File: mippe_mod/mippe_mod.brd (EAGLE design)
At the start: 32.5 x 50 mm, 21 parts, among them J1 VCC, J12 BURNIN, J3 UART, J4 FTDI, SW1 BTN-PTS810, U1 LM340MPX-5.0230, U2 ATMEGA328P-AUR, Y1 16MHz

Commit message: finish module and diff module
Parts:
- added J5: VCC, scono:1X02
- added J6: GND, scono:1X02
- added TP1: TEST_POINTTHRU, scono:TEST_POINT
- J2: value (none) -> GND
- R1: value (none) -> 10k
- R2, R3: value 330R -> 500R
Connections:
- new net AREF: U2.20
- net 5V: now also TP1.1; no longer U2.20
- net GND: now also J6.1, J6.2
- net VCC: now also J5.1, J5.2
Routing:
- net VCC: track 13.7 -> 40.3 mm
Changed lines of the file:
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@@
 <layer number="45" name="Holes" color="3" fill="1" visible="no" active="yes"/>
 <layer number="46" name="Milling" color="3" fill="1" visible="no" active="yes"/>
-<layer number="47" name="Measures" color="15" fill="1" visible="no" active="yes"/>
+<layer number="47" name="Measures" color="15" fill="1" visible="yes" active="yes"/>
 <layer number="48" name="Document" color="7" fill="1" visible="yes" active="yes"/>
 <layer number="49" name="Reference" color="7" fill="1" visible="no" active="yes"/>
@@
 <wire x1="1.5" y1="50" x2="0" y2="48.5" width="0" layer="20"/>
 <wire x1="0" y1="48.5" x2="0" y2="35" width="0" layer="20"/>
-<text x="1.5" y="23.5" size="0.7" layer="21">VCC</text>
-<text x="29.25" y="23.5" size="0.7" layer="21">GND</text>
-<dimension x1="0" y1="7" x2="32.5" y2="7" x3="16.25" y3="-2.5" textsize="0.7" layer="21"/>
-<dimension x1="0" y1="0" x2="0" y2="50" x3="-3.25" y3="25" textsize="0.7" layer="21"/>
+<text x="1.5" y="17" size="0.7" layer="21">VCC</text>
+<text x="29.25" y="17" size="0.7" layer="21">GND</text>
+<dimension x1="0" y1="7" x2="32.5" y2="7" x3="16.25" y3="-2.5" textsize="2" layer="47"/>
+<dimension x1="0" y1="0" x2="0" y2="50" x3="-3.25" y3="25" textsize="2" layer="47"/>
+<dimension x1="3.5" y1="29.5" x2="29" y2="29.5" x3="16.25" y3="53.75" textsize="2" layer="47"/>
+<dimension x1="3.5" y1="29.5" x2="3.5" y2="46.5" x3="40.75" y3="38" textsize="2" layer="47"/>
 </plain>
 <attributes>
@@
 </element>
 <element name="C7" library="scono" library_urn="urn:adsk.eagle:library:14850048" package="0402-CAP" package3d_urn="urn:adsk.eagle:package:14850678/2" value="0.1uF" x="25.75" y="7.5" smashed="yes" rot="R180">
-<attribute name="NAME" x="27.02" y="6.738" size="0.508" layer="25" font="vector" ratio="10" rot="R180"/>
 <attribute name="PIE-INT-REF-NUM" value="CAPACITOR-GENERIC" x="-4.73" y="44.33" size="1.778" layer="27" rot="R180" display="off"/>
 <attribute name="VALUE" x="27.02" y="8.897" size="0.508" layer="27" font="vector" rot="R180"/>
@@
 </element>
 <element name="J12" library="scono" library_urn="urn:adsk.eagle:library:14850048" package="BURNIN" package3d_urn="urn:adsk.eagle:package:14850856/2" value="BURNIN" x="17.72" y="4.77" smashed="yes" rot="R180"/>
-<element name="J2" library="scono" library_urn="urn:adsk.eagle:library:14850048" package="1X02" package3d_urn="urn:adsk.eagle:package:38039/1" value="" x="30.25" y="22" smashed="yes" rot="R270">
+<element name="J2" library="scono" library_urn="urn:adsk.eagle:library:14850048" package="1X02" package3d_urn="urn:adsk.eagle:package:38039/1" value="GND" x="30.25" y="22" smashed="yes" rot="R270">
 <attribute name="VALUE" x="28.218" y="23.27" size="0.6096" layer="27" font="vector" ratio="20" rot="R270"/>
 </element>
@@
 <attribute name="VALUE" x="8.73" y="5.468" size="0.6096" layer="27" font="vector" ratio="20"/>
 </element>
-<element name="R1" library="scono" library_urn="urn:adsk.eagle:library:14850048" package="R0402" package3d_urn="urn:adsk.eagle:package:14850590/2" value="" x="22.5" y="14.25" smashed="yes" rot="R270">
+<element name="R1" library="scono" library_urn="urn:adsk.eagle:library:14850048" package="R0402" package3d_urn="urn:adsk.eagle:package:14850590/2" value="10k" x="22.5" y="14.25" smashed="yes" rot="R270">
 <attribute name="VALUE" x="21.484" y="15.52" size="0.508" layer="27" font="vector" rot="R270" align="top-left"/>
 </element>
-<element name="R2" library="scono" library_urn="urn:adsk.eagle:library:14850048" package="R0402" package3d_urn="urn:adsk.eagle:package:14850590/2" value="330R" x="21.25" y="11" smashed="yes" rot="R90">
+<element name="R2" library="scono" library_urn="urn:adsk.eagle:library:14850048" package="R0402" package3d_urn="urn:adsk.eagle:package:14850590/2" value="500R" x="21.25" y="11" smashed="yes" rot="R90">
 <attribute name="VALUE" x="22.266" y="9.73" size="0.508" layer="27" font="vector" rot="R90" align="top-left"/>
 </element>
-<element name="R3" library="scono" library_urn="urn:adsk.eagle:library:14850048" package="R0402" package3d_urn="urn:adsk.eagle:package:14850590/2" value="330R" x="11.25" y="11" smashed="yes" rot="R270">
+<element name="R3" library="scono" library_urn="urn:adsk.eagle:library:14850048" package="R0402" package3d_urn="urn:adsk.eagle:package:14850590/2" value="500R" x="11.25" y="11" smashed="yes" rot="R270">
 <attribute name="VALUE" x="10.234" y="12.27" size="0.508" layer="27" font="vector" rot="R270" align="top-left"/>
 </element>
@@
 </element>
 <element name="Y1" library="scono" package="XTAL500X320X130N" value="16MHz" x="26" y="22" smashed="yes" rot="R270" grouprefs="XTAL"/>
+<element name="J5" library="scono" library_urn="urn:adsk.eagle:library:14850048" package="1X02" package3d_urn="urn:adsk.eagle:package:38039/1" value="VCC" x="2" y="46" smashed="yes" rot="R45">
+<attribute name="VALUE" x="2.5388125" y="43.66513125" size="0.6096" layer="27" font="vector" ratio="20" rot="R45"/>
+</element>
+<element name="J6" library="scono" library_urn="urn:adsk.eagle:library:14850048" package="1X02" package3d_urn="urn:adsk.eagle:package:38039/1" value="GND" x="30.5" y="46" smashed="yes" rot="R135">
+<attribute name="VALUE" x="32.83486875" y="46.5388125" size="0.6096" layer="27" font="vector" ratio="20" rot="R135"/>
+</element>
+<element name="TP1" library="scono" library_urn="urn:adsk.eagle:library:14850048" package="TEST_POINT" package3d_urn="urn:adsk.eagle:package:14850798/1" value="TEST_POINTTHRU" x="5.5" y="6" smashed="yes"/>
 </elements>
 <signals>
@@
 <wire x1="11.627" y1="9" x2="11.25" y2="9" width="0.1524" layer="1"/>
 <via x="11.25" y="9" extent="1-16" drill="0.35"/>
+<contactref element="J6" pad="1"/>
+<contactref element="J6" pad="2"/>
 </signal>
 <signal name="SCL">
@@
 <via x="13.804075" y="24.554075" extent="1-16" drill="0.35"/>
 <wire x1="13.804075" y1="24.554075" x2="13.804075" y2="20.054075" width="0.1524" layer="16"/>
-<wire x1="13.2768" y1="19.5268" x2="13.804075" y2="20.054075" width="0.1524" layer="16"/>
+<wire x1="13.375" y1="19.625" x2="13.2768" y2="19.5268" width="0.1524" layer="16"/>
+<wire x1="13.375" y1="19.625" x2="13.804075" y2="20.054075" width="0.1524" layer="16"/>
 <wire x1="17.72" y1="2.23" x2="16.75" y2="3.2" width="0.1524" layer="16"/>
 <wire x1="16.75" y1="3.2" x2="16.75" y2="4.5" width="0.1524" layer="16"/>
 <wire x1="16.75" y1="4.5" x2="15.25" y2="6" width="0.1524" layer="16"/>
-<wire x1="13.7084" y1="7.98396875" x2="13.2768" y2="8.41556875" width="0.1524" layer="16"/>
-<wire x1="13.2768" y1="8.41556875" x2="13.2768" y2="19.5268" width="0.1524" layer="16"/>
-<wire x1="13.7084" y1="6.5416" x2="13.7084" y2="7.98396875" width="0.1524" layer="16"/>
-<wire x1="15.25" y1="6" x2="14.25" y2="6" width="0.1524" layer="16"/>
-<wire x1="14.25" y1="6" x2="13.7084" y2="6.5416" width="0.1524" layer="16"/>
+<wire x1="14.25" y1="6" x2="15.25" y2="6" width="0.1524" layer="16"/>
+<wire x1="13.2768" y1="19.5268" x2="13.2768" y2="8.9732" width="0.1524" layer="16"/>
+<wire x1="13.2768" y1="8.9732" x2="13.75" y2="8.5" width="0.1524" layer="16"/>
+<wire x1="13.75" y1="8.5" x2="13.75" y2="6.5" width="0.1524" layer="16"/>
+<wire x1="13.75" y1="6.5" x2="14.25" y2="6" width="0.1524" layer="16"/>
 </signal>
 <signal name="SCK">
@@
 <contactref element="U2" pad="6"/>
 <contactref element="U2" pad="18"/>
-<contactref element="U2" pad="20"/>
 <contactref element="J4" pad="4"/>
 <contactref element="U1" pad="3"/>
@@
 <wire x1="17.72" y1="4.77" x2="17.72" y2="7.4" width="0.1524" layer="16"/>
 <wire x1="17.72" y1="7.4" x2="17.62" y2="7.5" width="0.1524" layer="16"/>
+<contactref element="TP1" pad="1"/>
 </signal>
 <signal name="VCC">
@@
 <wire x1="8.9" y1="19.85" x2="6.75" y2="22" width="0.508" layer="1"/>
 <wire x1="2.25" y1="19.46" x2="2.25" y2="22" width="0.508" layer="1"/>
+<contactref element="J5" pad="2"/>
+<contactref element="J5" pad="1"/>
+<wire x1="3.79605" y1="47.79605" x2="2" y2="46" width="0.508" layer="1"/>
+<wire x1="2" y1="46" x2="2" y2="22.25" width="0.508" layer="1"/>
+<wire x1="2" y1="22.25" x2="2.25" y2="22" width="0.508" layer="1"/>
+</signal>
+<signal name="AREF">
+<contactref element="U2" pad="20"/>
 </signal>
 </signals>

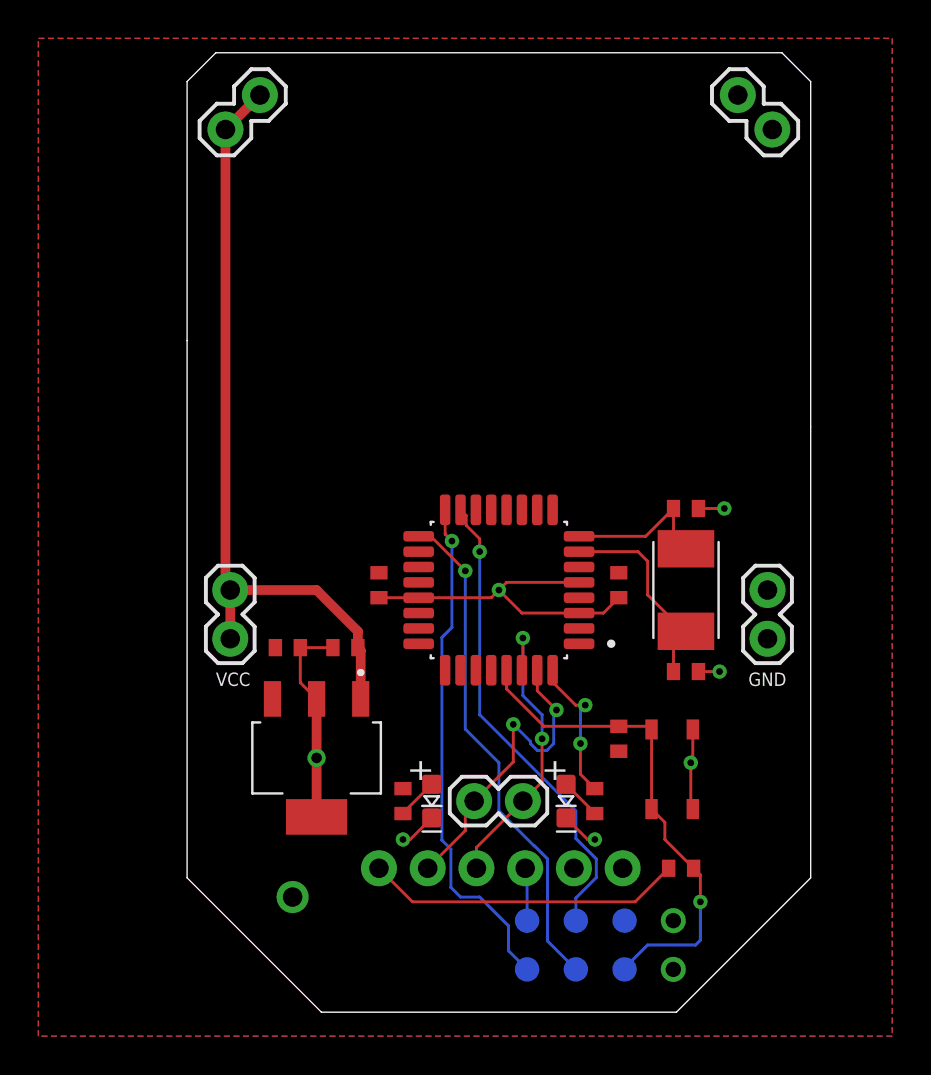
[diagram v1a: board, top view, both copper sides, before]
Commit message: finish bom cpl for mippe mod and adc diff
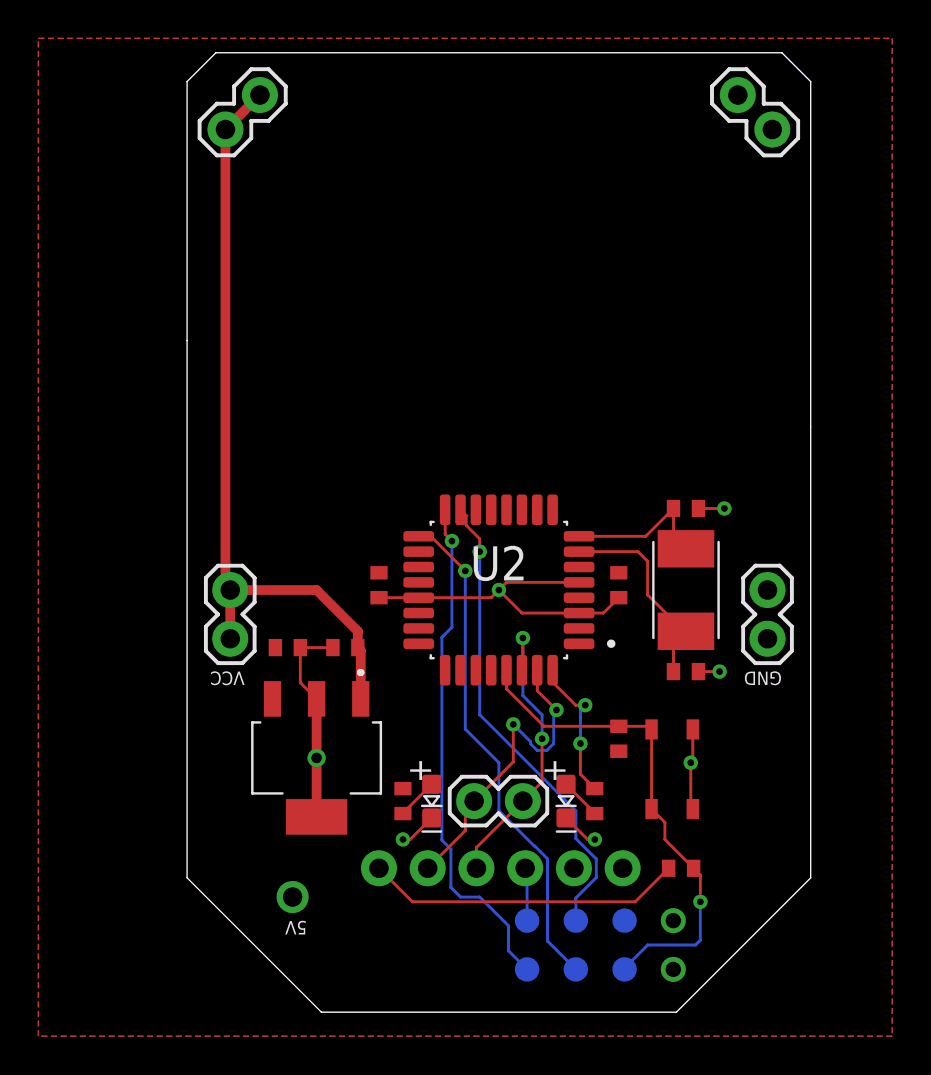
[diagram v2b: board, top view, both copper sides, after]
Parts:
- C7: value 0.1uF -> 100nF
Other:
- board text added: "5V"
- board text added: "U2"
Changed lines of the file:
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@@
 <wire x1="1.5" y1="50" x2="0" y2="48.5" width="0" layer="20"/>
 <wire x1="0" y1="48.5" x2="0" y2="35" width="0" layer="20"/>
-<text x="1.5" y="17" size="0.7" layer="21">VCC</text>
-<text x="29.25" y="17" size="0.7" layer="21">GND</text>
+<text x="3" y="17.75" size="0.7" layer="21" rot="SR180">VCC</text>
+<text x="31" y="17.75" size="0.7" layer="21" rot="SR180">GND</text>
 <dimension x1="0" y1="7" x2="32.5" y2="7" x3="16.25" y3="-2.5" textsize="2" layer="47"/>
 <dimension x1="0" y1="0" x2="0" y2="50" x3="-3.25" y3="25" textsize="2" layer="47"/>
 <dimension x1="3.5" y1="29.5" x2="29" y2="29.5" x3="16.25" y3="53.75" textsize="2" layer="47"/>
 <dimension x1="3.5" y1="29.5" x2="3.5" y2="46.5" x3="40.75" y3="38" textsize="2" layer="47"/>
+<text x="14.75" y="22.5" size="1.778" layer="25">U2</text>
+<text x="6.25" y="4.75" size="0.7" layer="25" rot="SR180">5V</text>
 </plain>
 <attributes>
@@
 <attribute name="PIE-INT-REF-NUM" value="CAPACITOR-GENERIC" x="51.4" y="-10.58" size="1.778" layer="27" display="off"/>
 </element>
-<element name="C7" library="scono" library_urn="urn:adsk.eagle:library:14850048" package="0402-CAP" package3d_urn="urn:adsk.eagle:package:14850678/2" value="0.1uF" x="25.75" y="7.5" smashed="yes" rot="R180">
+<element name="C7" library="scono" library_urn="urn:adsk.eagle:library:14850048" package="0402-CAP" package3d_urn="urn:adsk.eagle:package:14850678/2" value="100nF" x="25.75" y="7.5" smashed="yes" rot="R180">
 <attribute name="PIE-INT-REF-NUM" value="CAPACITOR-GENERIC" x="-4.73" y="44.33" size="1.778" layer="27" rot="R180" display="off"/>
 <attribute name="VALUE" x="27.02" y="8.897" size="0.508" layer="27" font="vector" rot="R180"/>

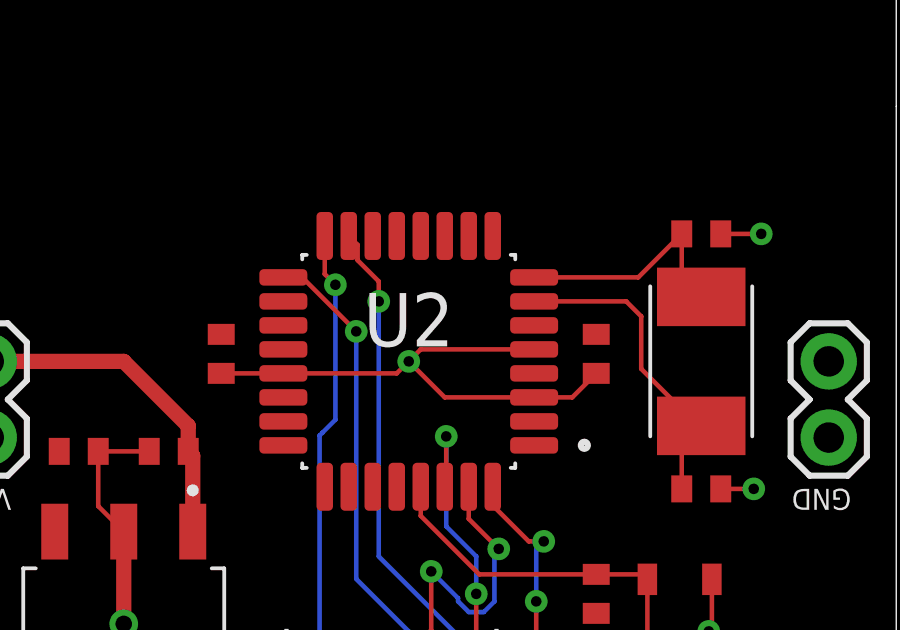
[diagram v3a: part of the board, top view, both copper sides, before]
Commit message: start oled pmic module
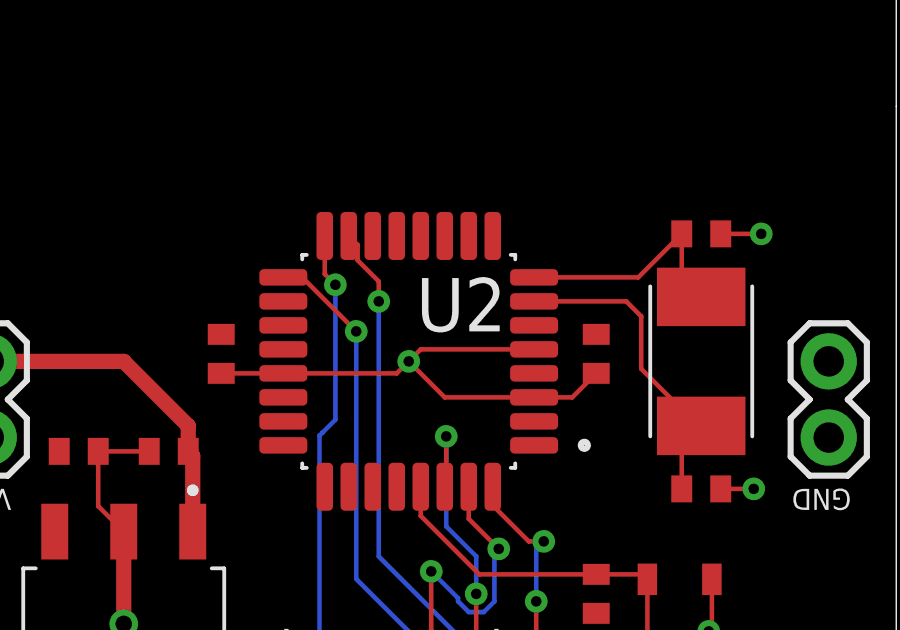
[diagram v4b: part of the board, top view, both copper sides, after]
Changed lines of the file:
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@@
 <layer number="45" name="Holes" color="3" fill="1" visible="no" active="yes"/>
 <layer number="46" name="Milling" color="3" fill="1" visible="no" active="yes"/>
-<layer number="47" name="Measures" color="15" fill="1" visible="yes" active="yes"/>
+<layer number="47" name="Measures" color="15" fill="1" visible="no" active="yes"/>
 <layer number="48" name="Document" color="7" fill="1" visible="yes" active="yes"/>
 <layer number="49" name="Reference" color="7" fill="1" visible="no" active="yes"/>
@@
 <dimension x1="3.5" y1="29.5" x2="29" y2="29.5" x3="16.25" y3="53.75" textsize="2" layer="47"/>
 <dimension x1="3.5" y1="29.5" x2="3.5" y2="46.5" x3="40.75" y3="38" textsize="2" layer="47"/>
-<text x="14.75" y="22.5" size="1.778" layer="25">U2</text>
+<text x="16.5" y="23" size="1.778" layer="25">U2</text>
 <text x="6.25" y="4.75" size="0.7" layer="25" rot="SR180">5V</text>
 <dimension x1="7" y1="0" x2="25.5" y2="0" x3="16.25" y3="-8.25" textsize="1.778" layer="47"/>
